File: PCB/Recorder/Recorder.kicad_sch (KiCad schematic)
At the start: 53 parts, among them J1 Battery, J2 Reset, J3 TC2030-USB-NL-DS, J4 TF_PUSH, J5 USB-C-Socket-H, Q2 CJ2301, SW1 SW_Push, U1 R, U2 ESP32-S3-MINI-1, U2 L, U3 TP4054, U4 ME6211C33M5G-N, U5 MAX98357A

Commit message: Tidy SS
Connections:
- net SCK: now also U2.9 (GPIO5); no longer U2.14 (GPIO10)
- net BLINK2 renamed LEDMIC
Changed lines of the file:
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@@
 	)
 	(no_connect
-		(at 35.56 60.96)
+		(at 35.56 73.66)
 	)
 	(no_connect
@@
 	(global_label "SCK"
 		(shape output)
-		(at 35.56 73.66 180)
-		(fields_autoplaced yes)
-		(effects
-			(font
-				(size 1.27 1.27)
-			)
-			(justify right)
-		)
-		(property "Intersheetrefs" "${INTERSHEET_REFS}"
-			(at 29.4795 73.66 0)
+		(at 35.56 60.96 180)
+		(fields_autoplaced yes)
+		(effects
+			(font
+				(size 1.27 1.27)
+			)
+			(justify right)
+		)
+		(property "Intersheetrefs" "${INTERSHEET_REFS}"
+			(at 29.4795 60.96 0)
 			(effects
 				(font
@@
 		)
 	)
-	(global_label "BLINK2"
+	(global_label "LEDMIC"
 		(shape output)
 		(at 35.56 68.58 180)
@@
 		)
 		(property "Intersheetrefs" "${INTERSHEET_REFS}"
-			(at 26.5161 68.58 0)
+			(at 26.4557 68.58 0)
 			(effects
 				(font
@@
 		)
 	)
-	(global_label "BLINK2"
+	(global_label "LEDMIC"
 		(shape input)
 		(at 251.46 45.72 180)
@@
 		)
 		(property "Intersheetrefs" "${INTERSHEET_REFS}"
-			(at 242.4161 45.72 0)
-			(effects
-				(font
+			(at 242.3557 45.72 0)
+			(effects
+				(font

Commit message: Fix component size
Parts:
- C11, C7: LCSC Part # C194427 -> C15525
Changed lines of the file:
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@@
 			)
 		)
-		(property "LCSC Part #" "C194427"
+		(property "LCSC Part #" "C15525"
 			(at 74.295 132.715 0)
 			(effects
@@
 			)
 		)
-		(property "LCSC Part #" "C194427"
+		(property "LCSC Part #" "C15525"
 			(at 91.44 133.35 0)
 			(effects

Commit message: Hook
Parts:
- C12, C14, R4, U5: now not fitted
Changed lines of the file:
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@@
 		(in_bom yes)
 		(on_board yes)
-		(dnp no)
+		(dnp yes)
 		(property "Reference" "C14"
 			(at 105.283 165.989 0)
@@
 		(in_bom yes)
 		(on_board yes)
-		(dnp no)
+		(dnp yes)
 		(fields_autoplaced yes)
 		(property "Reference" "U5"
@@
 		(in_bom yes)
 		(on_board yes)
-		(dnp no)
+		(dnp yes)
 		(property "Reference" "C12"
 			(at 92.329 165.862 0)
@@
 		(in_bom yes)
 		(on_board yes)
-		(dnp no)
+		(dnp yes)
 		(property "Reference" "R4"
 			(at 82.55 171.45 90)

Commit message: Tidy
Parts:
- U1, U2: footprint RevK:ICS43434_MEMS_Mic -> RevK:ICS43434_MEMS_Mic_Open
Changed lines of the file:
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@@
 			)
 		)
-		(property "Footprint" "RevK:ICS43434_MEMS_Mic"
+		(property "Footprint" "RevK:ICS43434_MEMS_Mic_Open"
 			(at 216.916 42.545 0)
 			(effects
@@
 			)
 		)
-		(property "Footprint" "RevK:ICS43434_MEMS_Mic"
+		(property "Footprint" "RevK:ICS43434_MEMS_Mic_Open"
 			(at 216.916 73.66 0)
 			(effects

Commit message: Allow all data on SD card maybe
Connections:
- net CHARGING: now also U2.15 (GPIO11); no longer U2.22 (GPIO18)
- net SDCD: now also U2.22 (GPIO18); no longer U2.21 (GPIO17)
- net SDDAT1: now also U2.21 (GPIO17); no longer U2.20 (GPIO16)
- net SDMISO: now also U2.20 (GPIO16); no longer U2.19 (GPIO15)
- net SDMOSI: now also U2.18 (GPIO14); no longer U2.17 (GPIO13)
- net SDSCK: now also U2.19 (GPIO15); no longer U2.18 (GPIO14)
- net SDSS: now also U2.17 (GPIO13); no longer U2.16 (GPIO12)
- net SDDAT2: now reaches J4.1 (DAT2), R14.2
- net SDDAT2: now also U2.16 (GPIO12)
- no-connect marks 19 -> 18
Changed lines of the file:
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@@
+	)
+	(junction
+		(at 137.16 74.295)
+		(diameter 0)
+		(color 0 0 0 0)
 	)
 	(junction
@@
 	)
 	(no_connect
-		(at 35.56 76.2)
-	)
-	(no_connect
 		(at 66.04 66.04)
 	)
@@
 		(pts
 			(xy 217.17 101.6) (xy 239.395 101.6)
+		)
+		(stroke
+			(width 0)
+			(type default)
+		)
+	)
+	(wire
+		(pts
+			(xy 137.16 74.295) (xy 111.125 74.295)
 		)
 		(stroke
@@
 	(global_label "CHARGING"
 		(shape input)
-		(at 35.56 93.98 180)
-		(fields_autoplaced yes)
-		(effects
-			(font
-				(size 1.27 1.27)
-			)
-			(justify right)
-		)
-		(property "Intersheetrefs" "${INTERSHEET_REFS}"
-			(at 23.7946 93.98 0)
+		(at 35.56 76.2 180)
+		(fields_autoplaced yes)
+		(effects
+			(font
+				(size 1.27 1.27)
+			)
+			(justify right)
+		)
+		(property "Intersheetrefs" "${INTERSHEET_REFS}"
+			(at 23.7946 76.2 0)
 			(effects
 				(font
@@
 	(global_label "SDMOSI"
 		(shape output)
-		(at 35.56 81.28 180)
-		(fields_autoplaced yes)
-		(effects
-			(font
-				(size 1.27 1.27)
-			)
-			(justify right)
-		)
-		(property "Intersheetrefs" "${INTERSHEET_REFS}"
-			(at 26.1533 81.28 0)
+		(at 35.56 83.82 180)
+		(fields_autoplaced yes)
+		(effects
+			(font
+				(size 1.27 1.27)
+			)
+			(justify right)
+		)
+		(property "Intersheetrefs" "${INTERSHEET_REFS}"
+			(at 26.1533 83.82 0)
 			(effects
 				(font
@@
 		)
 	)
+	(global_label "SDDAT2"
+		(shape input)
+		(at 111.125 74.295 180)
+		(fields_autoplaced yes)
+		(effects
+			(font
+				(size 1.27 1.27)
+			)
+			(justify right)
+		)
+		(property "Intersheetrefs" "${INTERSHEET_REFS}"
+			(at 101.7788 74.295 0)
+			(effects
+				(font
+					(size 1.27 1.27)
+				)
+				(justify right)
+				(hide yes)
+			)
+		)
+	)
 	(global_label "SDSCK"
 		(shape output)
-		(at 35.56 83.82 180)
-		(fields_autoplaced yes)
-		(effects
-			(font
-				(size 1.27 1.27)
-			)
-			(justify right)
-		)
-		(property "Intersheetrefs" "${INTERSHEET_REFS}"
-			(at 27 83.82 0)
+		(at 35.56 86.36 180)
+		(fields_autoplaced yes)
+		(effects
+			(font
+				(size 1.27 1.27)
+			)
+			(justify right)
+		)
+		(property "Intersheetrefs" "${INTERSHEET_REFS}"
+			(at 27 86.36 0)
 			(effects
 				(font
@@
 	(global_label "SDMISO"
 		(shape input)
-		(at 35.56 86.36 180)
-		(fields_autoplaced yes)
-		(effects
-			(font
-				(size 1.27 1.27)
-			)
-			(justify right)
-		)
-		(property "Intersheetrefs" "${INTERSHEET_REFS}"
-			(at 26.1533 86.36 0)
+		(at 35.56 88.9 180)
+		(fields_autoplaced yes)
+		(effects
+			(font
+				(size 1.27 1.27)
+			)
+			(justify right)
+		)
+		(property "Intersheetrefs" "${INTERSHEET_REFS}"
+			(at 26.1533 88.9 0)
 			(effects
 				(font
@@
 	(global_label "SDSS"
 		(shape output)
-		(at 35.56 78.74 180)
-		(fields_autoplaced yes)
-		(effects
-			(font
-				(size 1.27 1.27)
-			)
-			(justify right)
-		)
-		(property "Intersheetrefs" "${INTERSHEET_REFS}"
-			(at 28.3305 78.74 0)
+		(at 35.56 81.28 180)
+		(fields_autoplaced yes)
+		(effects
+			(font
+				(size 1.27 1.27)
+			)
+			(justify right)
+		)
+		(property "Intersheetrefs" "${INTERSHEET_REFS}"
+			(at 28.3305 81.28 0)
 			(effects
 				(font
@@
 		)
 	)
+	(global_label "SDDAT2"
+		(shape output)
+		(at 35.56 78.74 180)
+		(fields_autoplaced yes)
+		(effects
+			(font
+				(size 1.27 1.27)
+			)
+			(justify right)
+		)
+		(property "Intersheetrefs" "${INTERSHEET_REFS}"
+			(at 26.2138 78.74 0)
+			(effects
+				(font
+					(size 1.27 1.27)
+				)
+				(justify right)
+				(hide yes)
+			)
+		)
+	)
 	(global_label "VBAT"
 		(shape bidirectional)
@@
 	(global_label "SDDAT1"
 		(shape passive)
-		(at 35.56 88.9 180)
-		(fields_autoplaced yes)
-		(effects
-			(font
-				(size 1.27 1.27)
-			)
-			(justify right)
-		)
-		(property "Intersheetrefs" "${INTERSHEET_REFS}"
-			(at 27.1663 88.9 0)
+		(at 35.56 91.44 180)
+		(fields_autoplaced yes)
+		(effects
+			(font
+				(size 1.27 1.27)
+			)
+			(justify right)
+		)
+		(property "Intersheetrefs" "${INTERSHEET_REFS}"
+			(at 27.1663 91.44 0)
 			(effects
 				(font
@@
 	(global_label "SDCD"
 		(shape input)
-		(at 35.56 91.44 180)
-		(fields_autoplaced yes)
-		(effects
-			(font
-				(size 1.27 1.27)
-			)
-			(justify right)
-		)
-		(property "Intersheetrefs" "${INTERSHEET_REFS}"
-			(at 28.2095 91.44 0)
-			(effects
-				(font
+		(at 35.56 93.98 180)
+		(fields_autoplaced yes)
+		(effects
+			(font
+				(size 1.27 1.27)
+			)
+			(justify right)
+		)
+		(property "Intersheetrefs" "${INTERSHEET_REFS}"
+			(at 28.2095 93.98 0)
+			(effects
+				(font

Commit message: Tidy
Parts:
- removed C12: 10uF, RevK:C_0402, symbol Device:C
- removed C14: 100nF, RevK:C_0402, symbol Device:C
- removed R4: 634K, RevK:R_0402, symbol Device:R
- removed TP1: +, RevK:SolderPadSmall, symbol Connector:TestPoint
- removed TP2: -, RevK:SolderPadSmall, symbol Connector:TestPoint
- removed U5: MAX98357A, RevK:WLP-1.437mmx1.347mm-0.21mm-ball, symbol RevK:MAX98357A
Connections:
- net SDMISO renamed SDDAT0
- net SDMOSI renamed SDCMD
- net SDSCK renamed SDCLK
- net SDSS renamed SDDAT3
- net SKPPWR: no longer names the net of U2.34 (GPIO38)
- net SKPSCK: no longer names the net of U2.32 (GPIO36)
- net SKPSD: no longer names the net of U2.33 (GPIO37)
- net SKPWS: no longer names the net of U2.31 (GPIO35)
- no-connect marks 18 -> 22

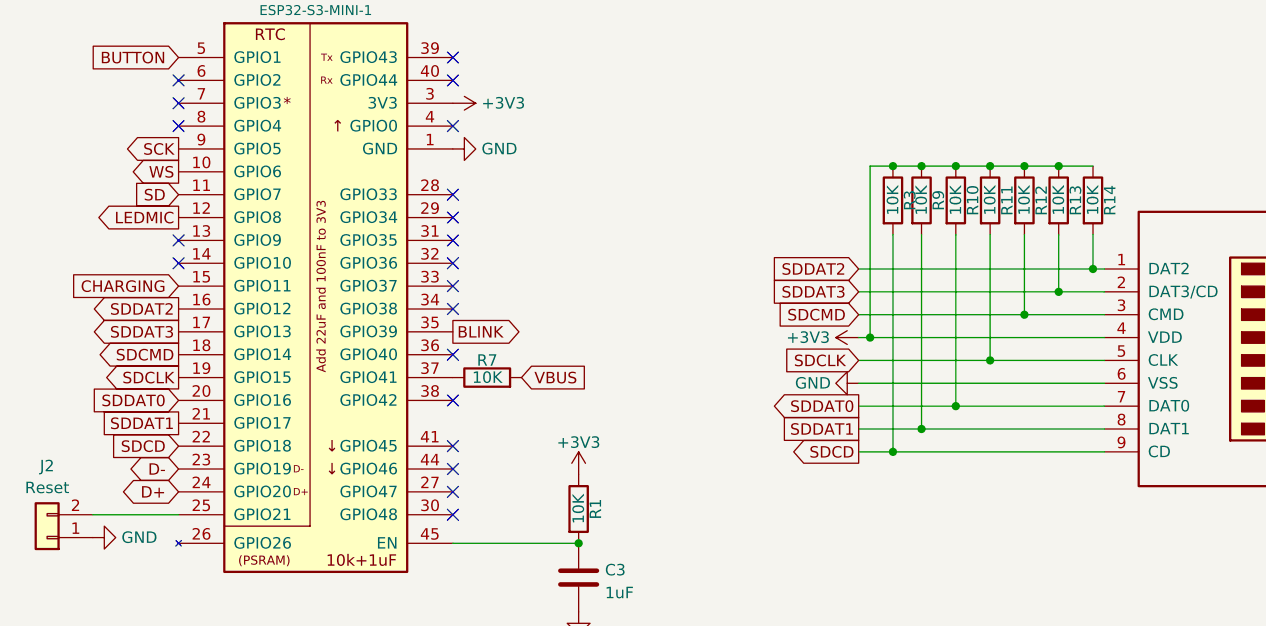
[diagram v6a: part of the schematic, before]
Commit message: Charging is 11 not 18 FFS
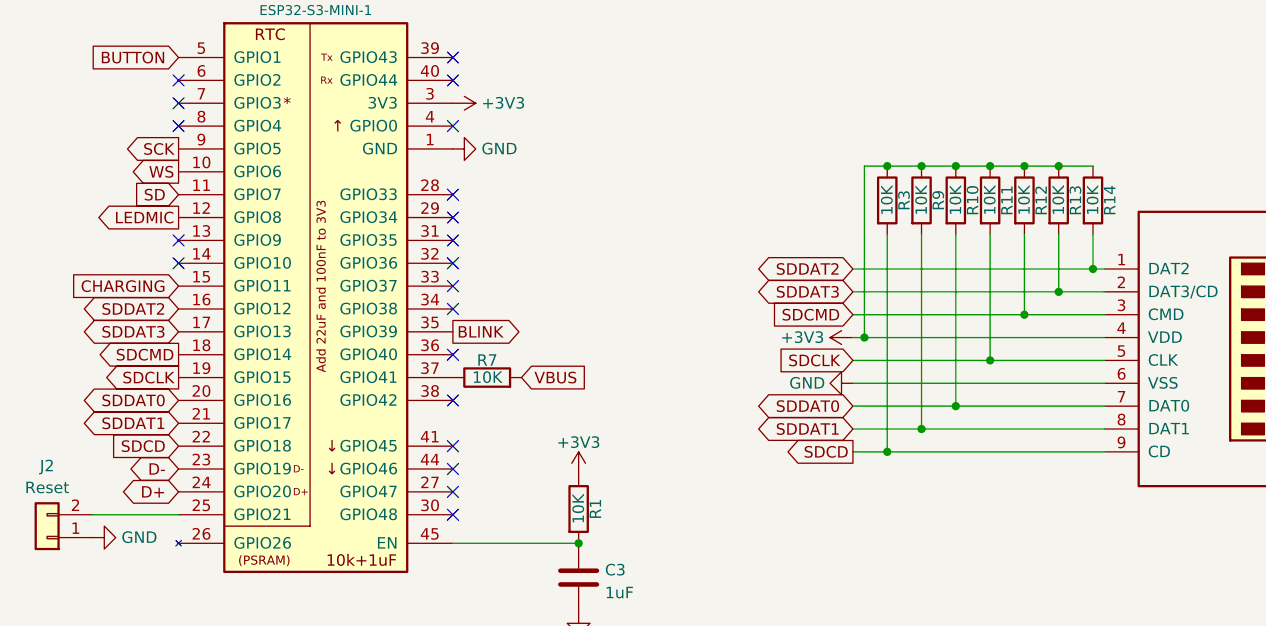
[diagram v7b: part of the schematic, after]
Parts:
- Q2: LCSC Part # C5224170 -> C8547
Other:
- moved on the sheet: R3
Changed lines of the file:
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@@
 	)
 	(junction
-		(at 114.935 94.615)
+		(at 114.3 94.615)
 		(diameter 0)
 		(color 0 0 0 0)
 	)
 	(junction
-		(at 114.935 62.865)
+		(at 114.3 62.865)
 		(diameter 0)
 		(color 0 0 0 0)
@@
 	)
 	(junction
-		(at 112.395 81.915)
+		(at 111.76 81.915)
 		(diameter 0)
 		(color 0 0 0 0)
@@
 	(wire
 		(pts
-			(xy 111.125 86.995) (xy 138.43 86.995)
+			(xy 110.49 86.995) (xy 138.43 86.995)
 		)
 		(stroke
@@
 	(wire
 		(pts
-			(xy 114.935 94.615) (xy 138.43 94.615)
+			(xy 114.3 94.615) (xy 138.43 94.615)
 		)
 		(stroke
@@
 	(wire
 		(pts
-			(xy 137.16 74.295) (xy 111.125 74.295)
+			(xy 137.16 74.295) (xy 110.49 74.295)
 		)
 		(stroke
@@
 	(wire
 		(pts
-			(xy 111.125 92.075) (xy 118.11 92.075)
+			(xy 110.49 92.075) (xy 118.11 92.075)
 		)
 		(stroke
@@
 	(wire
 		(pts
-			(xy 114.935 62.865) (xy 112.395 62.865)
+			(xy 114.3 62.865) (xy 111.76 62.865)
 		)
 		(stroke
@@
 	(wire
 		(pts
-			(xy 111.125 89.535) (xy 121.92 89.535)
+			(xy 110.49 89.535) (xy 121.92 89.535)
 		)
 		(stroke
@@
 	(wire
 		(pts
-			(xy 111.125 79.375) (xy 129.54 79.375)
+			(xy 110.49 79.375) (xy 129.54 79.375)
 		)
 		(stroke
@@
 	(wire
 		(pts
-			(xy 112.395 62.865) (xy 112.395 81.915)
+			(xy 111.76 62.865) (xy 111.76 81.915)
 		)
 		(stroke
@@
 	(wire
 		(pts
-			(xy 111.125 84.455) (xy 125.73 84.455)
+			(xy 110.49 84.455) (xy 125.73 84.455)
 		)
 		(stroke
@@
 	(wire
 		(pts
-			(xy 111.125 81.915) (xy 112.395 81.915)
+			(xy 110.49 81.915) (xy 111.76 81.915)
 		)
 		(stroke
@@
 	(wire
 		(pts
-			(xy 112.395 81.915) (xy 138.43 81.915)
+			(xy 111.76 81.915) (xy 138.43 81.915)
 		)
 		(stroke
@@
 	(wire
 		(pts
-			(xy 111.125 94.615) (xy 114.935 94.615)
+			(xy 110.49 94.615) (xy 114.3 94.615)
 		)
 		(stroke
@@
 	(wire
 		(pts
-			(xy 118.11 62.865) (xy 114.935 62.865)
+			(xy 118.11 62.865) (xy 114.3 62.865)
 		)
 		(stroke
@@
 	(wire
 		(pts
-			(xy 111.125 76.835) (xy 133.35 76.835)
+			(xy 110.49 76.835) (xy 133.35 76.835)
 		)
 		(stroke
@@
 	(wire
 		(pts
-			(xy 114.935 70.485) (xy 114.935 94.615)
+			(xy 114.3 70.485) (xy 114.3 94.615)
 		)
 		(stroke
@@
 	)
 	(global_label "SDDAT1"
-		(shape passive)
-		(at 111.125 92.075 180)
+		(shape bidirectional)
+		(at 110.49 92.075 180)
 		(fields_autoplaced yes)
 		(effects
@@
 		)
 		(property "Intersheetrefs" "${INTERSHEET_REFS}"
-			(at 102.7313 92.075 0)
+			(at 100.1913 92.075 0)
 			(effects
 				(font
@@
 	(global_label "SDCLK"
 		(shape input)
-		(at 111.125 84.455 180)
+		(at 110.49 84.455 180)
 		(fields_autoplaced yes)
 		(effects
@@
 		)
 		(property "Intersheetrefs" "${INTERSHEET_REFS}"
-			(at 102.7464 84.455 0)
+			(at 102.1114 84.455 0)
 			(effects
 				(font
@@
 	(global_label "SDCMD"
 		(shape input)
-		(at 111.125 79.375 180)
+		(at 110.49 79.375 180)
 		(fields_autoplaced yes)
 		(effects
@@
 		)
 		(property "Intersheetrefs" "${INTERSHEET_REFS}"
-			(at 102.3231 79.375 0)
+			(at 101.6881 79.375 0)
 			(effects
 				(font
@@
 	)
 	(global_label "SDDAT2"
-		(shape input)
-		(at 111.125 74.295 180)
+		(shape bidirectional)
+		(at 110.49 74.295 180)
 		(fields_autoplaced yes)
 		(effects
@@
 		)
 		(property "Intersheetrefs" "${INTERSHEET_REFS}"
-			(at 101.7788 74.295 0)
+			(at 100.1913 74.295 0)
 			(effects
 				(font
@@
 	)
 	(global_label "SDDAT0"
-		(shape input)
+		(shape bidirectional)
 		(at 35.56 88.9 180)
 		(fields_autoplaced yes)
@@
 		)
 		(property "Intersheetrefs" "${INTERSHEET_REFS}"
-			(at 26.2138 88.9 0)
+			(at 25.2613 88.9 0)
 			(effects
 				(font
@@
 	)
 	(global_label "SDDAT3"
-		(shape output)
+		(shape bidirectional)
 		(at 35.56 81.28 180)
 		(fields_autoplaced yes)
@@
 		)
 		(property "Intersheetrefs" "${INTERSHEET_REFS}"
-			(at 26.2138 81.28 0)
+			(at 25.2613 81.28 0)
 			(effects
 				(font
@@
 	)
 	(global_label "SDDAT2"
-		(shape output)
+		(shape bidirectional)
 		(at 35.56 78.74 180)
 		(fields_autoplaced yes)
@@
 		)
 		(property "Intersheetrefs" "${INTERSHEET_REFS}"
-			(at 26.2138 78.74 0)
+			(at 25.2613 78.74 0)
 			(effects
 				(font
@@
 	)
 	(global_label "SDDAT1"
-		(shape passive)
+		(shape bidirectional)
 		(at 35.56 91.44 180)
 		(fields_autoplaced yes)
@@
 		)
 		(property "Intersheetrefs" "${INTERSHEET_REFS}"
-			(at 27.1663 91.44 0)
+			(at 25.2613 91.44 0)
 			(effects
 				(font
@@
 	)
 	(global_label "SDDAT3"
-		(shape input)
-		(at 111.125 76.835 180)
+		(shape bidirectional)
+		(at 110.49 76.835 180)
 		(fields_autoplaced yes)
 		(effects
@@
 		)
 		(property "Intersheetrefs" "${INTERSHEET_REFS}"
-			(at 101.7788 76.835 0)
+			(at 100.1913 76.835 0)
 			(effects
 				(font
@@
 	(global_label "SDCD"
 		(shape output)
-		(at 111.125 94.615 180)
+		(at 110.49 94.615 180)
 		(fields_autoplaced yes)
 		(effects
@@
 		)
 		(property "Intersheetrefs" "${INTERSHEET_REFS}"
-			(at 103.7745 94.615 0)
+			(at 103.1395 94.615 0)
 			(effects
 				(font
@@
 	)
 	(global_label "SDDAT0"
-		(shape output)
-		(at 111.125 89.535 180)
+		(shape bidirectional)
+		(at 110.49 89.535 180)
 		(fields_autoplaced yes)
 		(effects
@@
 		)
 		(property "Intersheetrefs" "${INTERSHEET_REFS}"
-			(at 101.7788 89.535 0)
+			(at 100.1913 89.535 0)
 			(effects
 				(font
@@
 			)
 		)
-		(property "LCSC Part #" "C5224170"
+		(property "LCSC Part #" "C8547"
 			(at 180.975 128.905 90)
 			(effects
@@
 	(symbol
 		(lib_id "Device:R")
-		(at 114.935 66.675 0)
+		(at 114.3 66.675 0)
 		(unit 1)
 		(exclude_from_sim no)
@@
 		(dnp no)
 		(property "Reference" "R3"
-			(at 116.84 66.675 90)
+			(at 116.205 66.675 90)
 			(effects
 				(font
@@
 		)
 		(property "Value" "10K"
-			(at 114.935 66.675 90)
+			(at 114.3 66.675 90)
 			(effects
 				(font
@@
 		)
 		(property "Footprint" "RevK:R_0402"
-			(at 113.157 66.675 90)
+			(at 112.522 66.675 90)
 			(effects
 				(font
@@
 		)
 		(property "Datasheet" "~"
-			(at 114.935 66.675 0)
+			(at 114.3 66.675 0)
 			(effects
 				(font
@@
 		)
 		(property "Description" ""
-			(at 114.935 66.675 0)
+			(at 114.3 66.675 0)
 			(effects
 				(font
@@
 	(symbol
 		(lib_id "power:GND")
-		(at 111.125 86.995 270)
+		(at 110.49 86.995 270)
 		(unit 1)
 		(exclude_from_sim no)
@@
 		(dnp no)
 		(property "Reference" "#PWR028"
-			(at 104.775 86.995 0)
+			(at 104.14 86.995 0)
 			(effects
 				(font
@@
 		)
 		(property "Value" "GND"
-			(at 106.045 86.995 90)
+			(at 105.41 86.995 90)
 			(effects
 				(font
@@
 		)
 		(property "Footprint" ""
-			(at 111.125 86.995 0)
+			(at 110.49 86.995 0)
 			(effects
 				(font
@@
 		)
 		(property "Datasheet" ""
-			(at 111.125 86.995 0)
+			(at 110.49 86.995 0)
 			(effects
 				(font
@@
 		)
 		(property "Description" "Power symbol creates a global label with name \"GND\" , ground"
-			(at 111.125 86.995 0)
+			(at 110.49 86.995 0)
 			(effects
 				(font
@@
 	(symbol
 		(lib_id "power:+3.3V")
-		(at 111.125 81.915 90)
+		(at 110.49 81.915 90)
 		(unit 1)
 		(exclude_from_sim no)
@@
 		(fields_autoplaced yes)
 		(property "Reference" "#PWR03"
-			(at 114.935 81.915 0)
+			(at 114.3 81.915 0)
 			(effects
 				(font
@@
 		)
 		(property "Value" "+3V3"
-			(at 107.95 81.915 90)
+			(at 107.315 81.915 90)
 			(effects
 				(font
@@
 		)
 		(property "Footprint" ""
-			(at 111.125 81.915 0)
+			(at 110.49 81.915 0)
 			(effects
 				(font
@@
 		)
 		(property "Datasheet" ""
-			(at 111.125 81.915 0)
+			(at 110.49 81.915 0)
 			(effects
 				(font
@@
 		)
 		(property "Description" "Power symbol creates a global label with name \"+3.3V\""
-			(at 111.125 81.915 0)
+			(at 110.49 81.915 0)
 			(effects
 				(font
